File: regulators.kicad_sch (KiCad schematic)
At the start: 51 parts, among them SW1 SKRPANE010, U1 STM32H723ZGT6, U3 AP62300TWU, U4 AP2112K-3.3, Y1 25 MHz

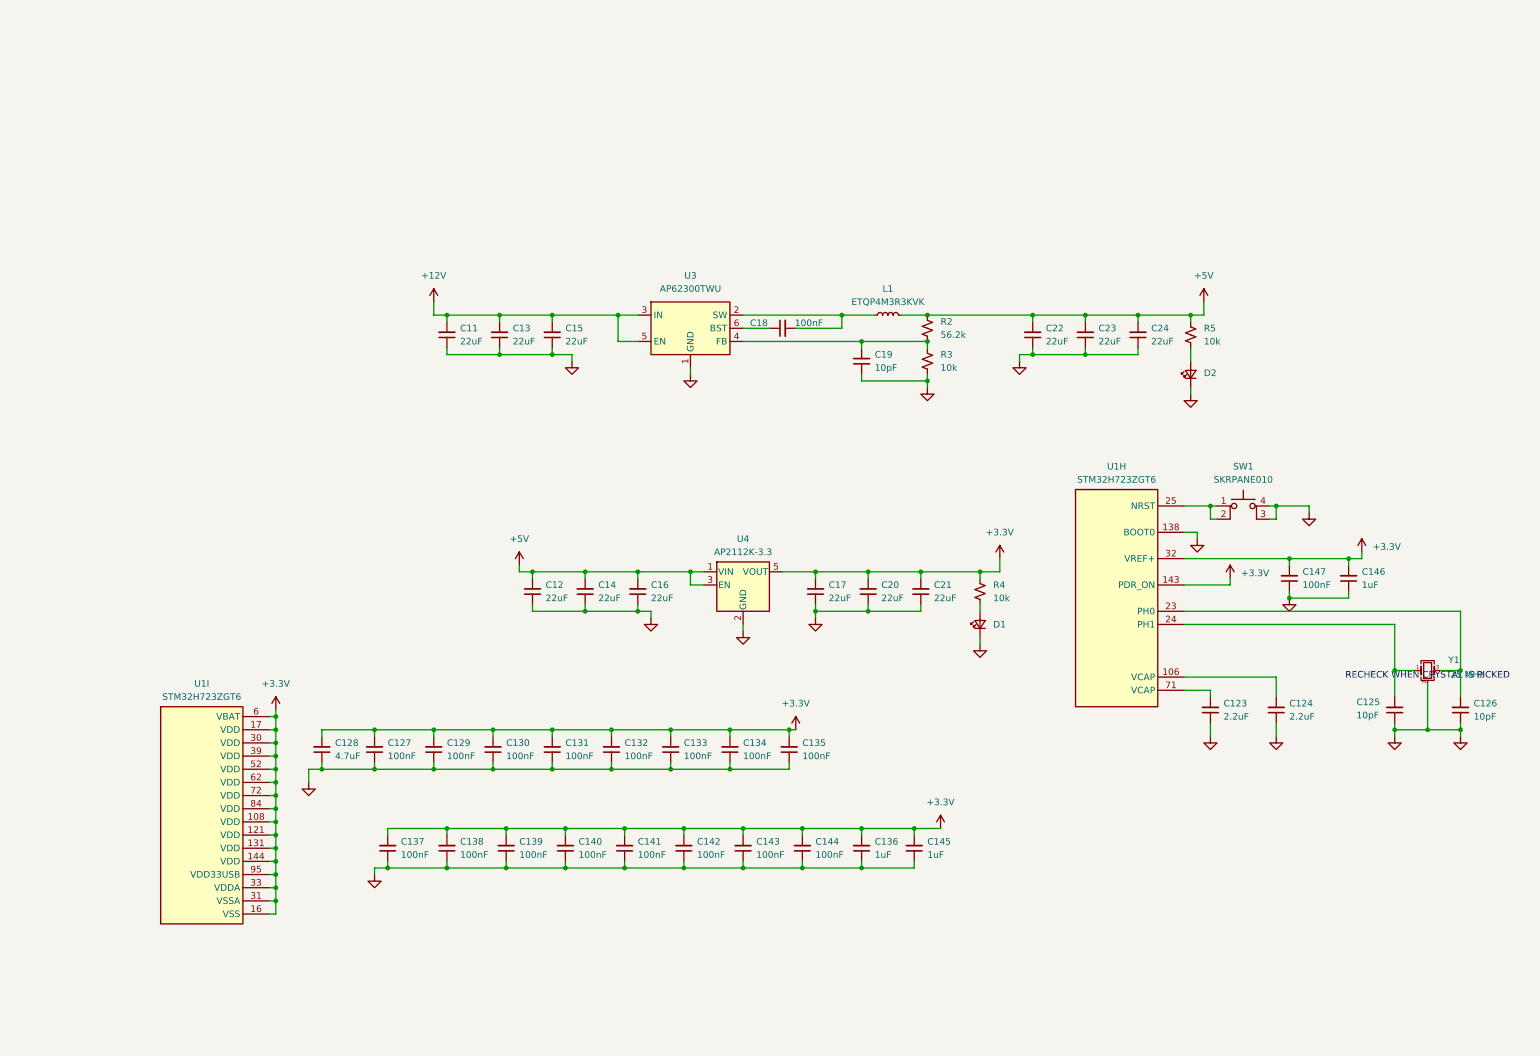
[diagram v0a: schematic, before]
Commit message: Soften scope, begin layout, reorganize sheets (still need to delete extras)
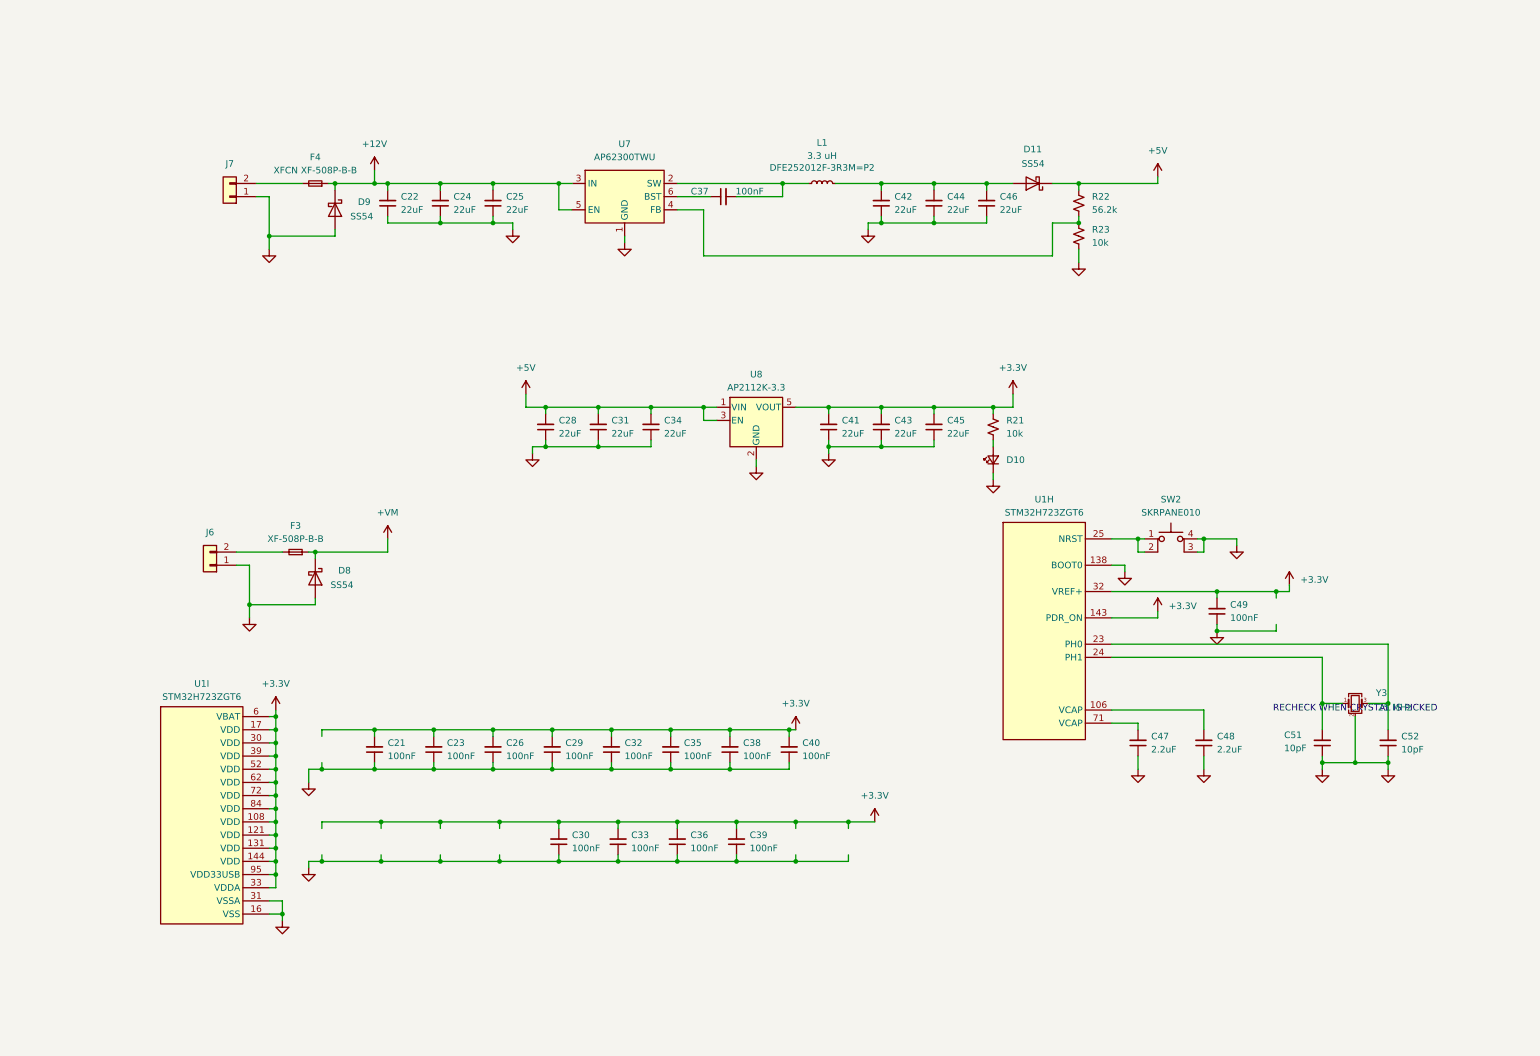
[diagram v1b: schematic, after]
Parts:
- removed C12, C14, C16, C17, C24: 22uF, symbol Device:C_Small
- removed C128: 4.7uF, symbol Device:C_Small
- removed C129, C137, C138, C139, C140: 100nF, symbol Device:C_Small
- removed C136, C145, C146: 1uF, symbol Device:C_Small
- removed C19: 10pF, symbol Device:C_Small
- removed D1, D2: LED_Small, symbol Device:LED_Small
- removed R4, R5: 10k, symbol Device:R_Small_US
- removed U3: AP62300TWU, Package_TO_SOT_SMD:TSOT-23-6, symbol Regulator_Switching:AP62300TWU
- removed U4: AP2112K-3.3, Package_TO_SOT_SMD:SOT-23-5, symbol Regulator_Linear:AP2112K-3.3
- added C23: 100nF, APRLPrints:C_0603, symbol Device:C_Small
- added C28, C31, C34, C41, C46: 22uF, APRLPrints:C_0805, symbol Device:C_Small
- added D10: LED_Small, APRLPrints:LED_0603, symbol Device:LED_Small
- added D11, D8, D9: SS54, Diode_SMD:D_SMA, symbol Diode:SS38
- added F3: XF-508P-B-B, Fuse:Fuseholder_Blade_Mini_Keystone_3568, symbol Device:Fuse_Small
- added F4: XFCN XF-508P-B-B, Fuse:Fuseholder_Blade_Mini_Keystone_3568, symbol Device:Fuse_Small
- added J6, J7: Screw_Terminal_01x02, Connector_Phoenix_MSTB:PhoenixContact_MSTBA_2,5_2-G_1x02_P5.00mm_Horizontal, symbol Connector_Generic:Conn_01x02
- added R21: 10k, APRLPrints:R_0603, symbol Device:R_Small_US
- added U7: AP62300TWU, Package_TO_SOT_SMD:TSOT-23-6, symbol Regulator_Switching:AP62300TWU
- added U8: AP2112K-3.3, Package_TO_SOT_SMD:SOT-23-5, symbol Regulator_Linear:AP2112K-3.3
- C21: renamed from C127; footprint (none) -> APRLPrints:C_0603
- C22: renamed from C11; footprint (none) -> APRLPrints:C_0805
- C24: renamed from C13; footprint (none) -> APRLPrints:C_0805
- C25: renamed from C15; footprint (none) -> APRLPrints:C_0805
- C26: renamed from C130; footprint (none) -> APRLPrints:C_0603
- C29: renamed from C131; footprint (none) -> APRLPrints:C_0603
- C30: renamed from C141; footprint (none) -> APRLPrints:C_0603
- C32: renamed from C132; footprint (none) -> APRLPrints:C_0603
- C33: renamed from C142; footprint (none) -> APRLPrints:C_0603
- C35: renamed from C133; footprint (none) -> APRLPrints:C_0603
- C36: renamed from C143; footprint (none) -> APRLPrints:C_0603
- C37: renamed from C18; footprint (none) -> APRLPrints:C_0603
- C38: renamed from C134; footprint (none) -> APRLPrints:C_0603
- C39: renamed from C144; footprint (none) -> APRLPrints:C_0603
- C40: renamed from C135; footprint (none) -> APRLPrints:C_0603
- C42: renamed from C22; footprint (none) -> APRLPrints:C_0805
- C43: renamed from C20; footprint (none) -> APRLPrints:C_0805
- C44: renamed from C23; footprint (none) -> APRLPrints:C_0805
- C45: renamed from C21; footprint (none) -> APRLPrints:C_0805
- C47: renamed from C123; footprint (none) -> APRLPrints:C_0603
- C48: renamed from C124; footprint (none) -> APRLPrints:C_0603
- C49: renamed from C147; footprint (none) -> APRLPrints:C_0603
- C51: renamed from C125; footprint (none) -> APRLPrints:C_0603
- C52: renamed from C126; footprint (none) -> APRLPrints:C_0603
- L1: value ETQP4M3R3KVK -> 3.3 uH; footprint Inductor_SMD:L_Panasonic_PCC-M0850M -> Inductor_SMD:L_1008_2520Metric; Part # (none) -> DFE252012F-3R3M=P2
- R22: renamed from R2; footprint (none) -> APRLPrints:R_0603
- R23: renamed from R3; footprint (none) -> APRLPrints:R_0603
- SW2: renamed from SW1; footprint (none) -> APRLPrints:SKRPANE010
- Y3: renamed from Y1; footprint (none) -> APRLPrints:3225-4P-L; private KLC_S4.1 -> (none)
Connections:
- net +12V: now also D9.1 (K), F4.1, U7.3 (IN), U7.5 (EN)
- net +3.3V: now also C23.2, C41.2, R21.1, U8.5 (VOUT); no longer U1.107 (VSS), U1.120 (VSS), U1.130 (VSS), U1.16 (VSS), U1.31 (VSSA), U1.38 (VSS), U1.51 (VSS), U1.61 (VSS), U1.83 (VSS), U1.94 (VSS)
- net +5V: now also C28.2, C31.2, C34.2, D11.1 (K), U8.1 (VIN), U8.3 (EN); no longer C42.2, C44.2, L1.2
- net GND: now also U1.107 (VSS), U1.120 (VSS), U1.130 (VSS), U1.16 (VSS), U1.31 (VSSA), U1.38 (VSS), U1.51 (VSS), U1.61 (VSS), U1.83 (VSS), U1.94 (VSS), C23.1, C28.1, C31.1, C34.1, C41.1, C46.1, D10.1 (K), D8.2 (A), D9.2 (A), J6.1 (Pin_1), J7.1 (Pin_1), U7.1 (GND), U8.2 (GND)
- net at R22.2, R23.1: now also U7.4 (FB)
- net at C37.1: now also U7.6 (BST)
- net at C37.2, L1.1: now also U7.2 (SW)
- new net: F3.2, J6.2 (Pin_2)
- new net: C42.2, C44.2, C46.2, D11.2 (A), L1.2
- new net: F4.2, J7.2 (Pin_2)
- new net: D10.2 (A), R21.2
- new net +VM: D8.1 (K), F3.1
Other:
- moved on the sheet: C22, C24, C25, C30, C33, C36, C37, C39, C42, C43, C44, C45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
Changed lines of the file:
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@@
 	(generator "eeschema")
 	(generator_version "9.0")
-	(paper "A4")
+	(paper "USLetter")
 	(title_block
 		(title "Serie Mainboard")

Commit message: ???
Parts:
- removed C21, C23, C26: 100nF, APRLPrints:C_0603, symbol Device:C_Small
- removed C22, C24, C25: 22uF, APRLPrints:C_0805, symbol Device:C_Small
- removed D11, D9: SS54, Diode_SMD:D_SMA, symbol Diode:SS38
- removed F4: XFCN XF-508P-B-B, Fuse:Fuseholder_Blade_Mini_Keystone_3568, symbol Device:Fuse_Small
- removed J6, J7: Screw_Terminal_01x02, Connector_Phoenix_MSTB:PhoenixContact_MSTBA_2,5_2-G_1x02_P5.00mm_Horizontal, symbol Connector_Generic:Conn_01x02
- removed L1: 3.3 uH, Inductor_SMD:L_1008_2520Metric, symbol Device:L_Small
- removed U1: STM32H723ZGT6, Package_QFP:LQFP-144_20x20mm_P0.5mm, symbol libserie:STM32H723ZGTx
- removed U7: AP62300TWU, Package_TO_SOT_SMD:TSOT-23-6, symbol Regulator_Switching:AP62300TWU
- removed U8: AP2112K-3.3, Package_TO_SOT_SMD:SOT-23-5, symbol Regulator_Linear:AP2112K-3.3
- added C27: 22uF, APRLPrints:C_0805, symbol Device:C_Small
- added C50: 100nF, symbol Device:C_Small
- added C53, C54, C56, C57, C59, C60, C61, C65: 22uF, symbol Device:C_Small
- added C55, C58, C62, C63, C64, C66, C67: 100nF, APRLPrints:C_0603, symbol Device:C_Small
- added D6: SS54, Diode_SMD:D_SMA, symbol Diode:SS38
- added D7, D9: LED_Small, APRLPrints:LED_0603, symbol Device:LED_Small
- added F2: XFCN XF-508P-B-B, Fuse:Fuseholder_Blade_Mini_Keystone_3568, symbol Device:Fuse_Small
- added J15: Screw_Terminal_06x01x02, TerminalBlock_Ningbo-Kagnex:TerminalBlock_Ningbo-Kagnex_HB9500M_1x12_P9.5mm, symbol libserie:Screw_Terminal_06x01x02
- added L1: 3.6 uH, symbol Device:L
- added L2: 10 uH, symbol Device:L
- added R18, R19: 200k, symbol Device:R_Small_US
- added R20: 15.8k, symbol Device:R_Small_US
- added R24, R26: 22.1k, symbol Device:R_Small_US
- added R25: 309k, symbol Device:R_Small_US
- added R27, R28: 10k, APRLPrints:R_0603, symbol Device:R_Small_US
- added U13: STM32H723ZGT6, Package_QFP:LQFP-144_20x20mm_P0.5mm, symbol libserie:STM32H723ZGTx
- added U14: AP2112K-3.3, Package_TO_SOT_SMD:SOT-23-5, symbol Regulator_Linear:AP2112K-3.3
- added U15, U16: AP64500, Package_SO:Diodes_SO-8EP, symbol libserie:AP64500-EP
- added U17: TPS7A20xxxDQN, Package_SON:Texas_X2SON-4_1x1mm_P0.65mm, symbol Regulator_Linear:TPS7A20xxxDQN
- C28, C31: value 22uF -> 2.2uF; footprint APRLPrints:C_0805 -> APRLPrints:C_0603
- C29, C30, C38: value 100nF -> 22uF; footprint APRLPrints:C_0603 -> APRLPrints:C_0805
- C33, C36, C37, C40: value 100nF -> 22uF; footprint APRLPrints:C_0603 -> (none)
- C34, C41: footprint APRLPrints:C_0805 -> (none)
- C35, C39: value 100nF -> 10pF
- C44, C45: value 22uF -> 2.7nF; footprint APRLPrints:C_0805 -> (none)
- C46: value 22uF -> 100nF; footprint APRLPrints:C_0805 -> APRLPrints:C_0603
- C47, C48: value 2.2uF -> 100nF
- C49: footprint APRLPrints:C_0603 -> (none)
- C51, C52: value 10pF -> 100nF
- R21: value 10k -> 37.4k; footprint APRLPrints:R_0603 -> (none)
- R22: value 56.2k -> 10k
- R23: value 10k -> 115k; footprint APRLPrints:R_0603 -> (none)
- Y1: renamed from Y3; private (none) -> KLC_S4.1
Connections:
- net +12V: now also C54.1, C57.1, C60.1, L2.2, R25.1, R28.1
- net +3.3V: now also C42.2, C46.2, C47.2, C48.2, C51.2, C52.2, R22.1, C55.2, C58.2, C62.2, C63.2, C64.2, C66.2, C67.2, U13.41 (PA5), U13.43 (PA7), U14.5 (VOUT); no longer C29.2, C30.2, C33.2, C35.2, C36.2, C39.2, C40.2, C41.2, C45.2, C49.2, R21.1
- net +5V: now also C29.2, C30.2, R23.1, C27.2, C53.1, C56.1, C59.1, C61.1, L1.2, R27.1, U14.1 (VIN), U14.3 (EN), U17.3 (EN), U17.4 (IN); no longer C28.2, C31.2, C34.2, R22.1
- net GND: now also C33.2, C34.2, C36.2, C37.2, C40.2, C41.2, C44.2, C45.2, C27.1, C53.2, C54.2, C55.1, C56.2, C57.2, C58.1, C59.2, C60.2, C61.2, C62.1, C63.1, C64.1, C65.2, C66.1, C67.1, D6.2 (A), D7.1 (K), D9.1 (K), J15.1 (Pin_1), J15.3 (Pin_1), R18.2, R19.2, R24.2, R26.2, U13.37 (PA3), U14.2 (GND), U15.7 (GND), U15.9 (EP), U16.7 (GND), U16.9 (EP), U17.2 (GND), U17.5 (Pad); no longer C33.1, C34.1, C36.1, C40.1, C41.1, C44.1, C45.1, C49.1, R23.2
- net at R22.2: now also D7.2 (A); no longer R23.1
- net at F3.2: now also J15.4 (Pin_2)
- net at Y1.1: now also C35.2, U13.102 (PA10); no longer C51.2
- net +24V: now reaches C37.1
- net +24V: now also C33.1, C34.1, C36.1, C40.1, C41.1, D6.1 (K), F2.1, U15.2 (VIN), U15.3 (EN), U16.2 (VIN), U16.3 (EN)
- net at SW2.1, SW2.2: now also U13.35 (PA1)
- net at Y1.3: now also C39.2, U13.101 (PA9); no longer C52.2
- net at R21.2: now also C45.1; no longer D10.2 (A)
- new net: C49.2, L1.1, U15.8 (SW)
- new net: R23.2, R24.1, U15.5 (FB)
- new net: D10.2 (A), R28.2
- new net: D9.2 (A), R27.2
- new net: C49.1, U15.1 (BST)
- new net: R18.1, U15.4 (RT/CLK)
- new net: R20.1, U15.6 (COMP)
- new net: C44.1, R20.2
- new net: C31.2, U13.109 (PA14(JTCK)
- new net: C28.2, U13.110 (PA15(JTDI))
- new net: R19.1, U16.4 (RT/CLK)
- new net: R21.1, U16.6 (COMP)
- new net: F2.2, J15.2 (Pin_2)
- new net: R25.2, R26.1, U16.5 (FB)
- new net: C50.1, U16.1 (BST)
- new net: C50.2, L2.1, U16.8 (SW)
- new net +4.5V: C65.1, U17.1 (OUT)
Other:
- note added: "24V -> 12V"
- note added: "24V -> 5V"
- note added: "3.3V Regulator"
- note added: "Motor Power"
- note added: "Power Inputs"
- note added: "Power Regulators"
- note added: "Precision 4.5V Regulator"
- note added: "This still needs a home"
- note removed: "RECHECK WHEN CRYSTAL IS PICKED"
- moved on the sheet: SW2, Y1

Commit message: loadcell math coming soon(tm)
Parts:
- removed C28, C31: 2.2uF, APRLPrints:C_0603, symbol Device:C_Small
- removed C32: 100nF, APRLPrints:C_0603, symbol Device:C_Small
- removed C35, C39: 10pF, APRLPrints:C_0603, symbol Device:C_Small
- removed unit 2 of J15
- removed SW2: SKRPANE010, APRLPrints:SKRPANE010, symbol Switch:SW_MEC_5E
- removed U13: STM32H723ZGT6, Package_QFP:LQFP-144_20x20mm_P0.5mm, symbol libserie:STM32H723ZGTx
- removed Y1: 25 MHz, APRLPrints:3225-4P-L, symbol Device:Crystal_GND24_Small
- added D20: SS54, Diode_SMD:D_SMA, symbol Diode:SS38
- added unit 2 of J14
- C32: renamed from C50; footprint (none) -> APRLPrints:C_0603
- C33: renamed from C34; footprint (none) -> APRLPrints:C_0805
- C34: renamed from C37; footprint (none) -> APRLPrints:C_0805
- C35: renamed from C41; footprint (none) -> APRLPrints:C_0805
- C36: renamed from C54; footprint (none) -> APRLPrints:C_0805
- C37: renamed from C57; footprint (none) -> APRLPrints:C_0805
- C38: renamed from C60; footprint (none) -> APRLPrints:C_0805
- C39: renamed from C45; value 2.7nF -> 1nF; footprint (none) -> APRLPrints:C_0603
- C40: renamed from C49; footprint (none) -> APRLPrints:C_0603
- C41: renamed from C33; footprint (none) -> APRLPrints:C_0805
- C42: renamed from C36; footprint (none) -> APRLPrints:C_0805
- C43: renamed from C40; footprint (none) -> APRLPrints:C_0805
- C44: renamed from C53; footprint (none) -> APRLPrints:C_0805
- C45: renamed from C56; footprint (none) -> APRLPrints:C_0805
- C46: renamed from C59; footprint (none) -> APRLPrints:C_0805
- C47: renamed from C44; value 2.7nF -> 1nF; footprint (none) -> APRLPrints:C_0603
- C54: renamed from C61; footprint (none) -> APRLPrints:C_0805
- C55: renamed from C65; footprint (none) -> APRLPrints:C_0805
- L1: renamed from L2; value 10 uH -> 6.8 uH; footprint (none) -> Inductor_SMD:L_Changjiang_FXL0630; Part # SLO1040H100MTT -> FXL0630-6R8-M
- L2: renamed from L1; value 3.6 uH -> 3.3 uH; footprint (none) -> Inductor_SMD:L_Changjiang_FXL0630; Part # GDIM1070-3R6MTF -> FXL0630-3R3-M
- R31: renamed from R25; value 309k -> 140k; footprint (none) -> APRLPrints:R_0603
- R32: renamed from R19; footprint (none) -> APRLPrints:R_0603
- R33: renamed from R21; value 37.4k -> 30.9k; footprint (none) -> APRLPrints:R_0603
- R34: renamed from R26; value 22.1k -> 10k; footprint (none) -> APRLPrints:R_0603
- R36: renamed from R23; value 115k -> 52.5k; footprint (none) -> APRLPrints:R_0603
- R37: renamed from R18; footprint (none) -> APRLPrints:R_0603
- R38: renamed from R20; value 15.8k -> 30.9k; footprint (none) -> APRLPrints:R_0603
- R39: renamed from R24; value 22.1k -> 10k; footprint (none) -> APRLPrints:R_0603
- renumbered C27 to C48, C29 to C49, C30 to C50, C38 to C51, C42 to C52, C43 to C53, C46 to C56, C47 to C57, C48 to C58, C51 to C59, C52 to C60, C55 to C61, C58 to C62, C62 to C63, C63 to C64, C64 to C65, D7 to D10, D10 to D7, D9 to D8, D8 to D9, J15 to J14, R28 to R30, R27 to R35, R22 to R40, U16 to U12, U15 to U13, U17 to U15
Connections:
- net +5V: now also D20.1 (K); no longer C44.1, C45.1, C46.1, L2.2
- net GND: now also J14.3 (Pin_1)
- net at F3.2: now also J14.4 (Pin_2)
- new net: C44.1, C45.1, C46.1, D20.2 (A), L2.2
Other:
- note removed: "This still needs a home"
- moved on the sheet: C48, C49, C50, C51, C52, C53, C54, C55, C56, C57, C58, C59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

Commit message: a
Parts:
- removed D6, D9: SS54, Diode_SMD:D_SMA, symbol Diode:SS38
- removed U12: AP64500, Package_SO:Diodes_SO-8EP, symbol libserie:AP64500-EP
- added C32, C42: 100uF, Capacitor_SMD:CP_Elec_10x10.5, symbol Device:C_Small
- added C36, C46, C56, C58, C59: 100nF, APRLPrints:C_0603, symbol Device:C_Small
- added C57: 1uF, APRLPrints:C_0603, symbol Device:C_Small
- added Q1, Q2, Q3: BSC016N06NS, Package_TO_SOT_SMD:TDSON-8-1, symbol Transistor_FET:CSD18532NQ5B
- added U11: AP64500, libserie:Diodes_SO-8EP, symbol libserie:AP64500-EP
- added U12, U14, U17: AP74700Q, libserie:SOT-6, symbol libserie:AP74700Q
- F2: value XFCN XF-508P-B-B -> XF-508P-B-B
- U13: footprint Package_SO:Diodes_SO-8EP -> libserie:Diodes_SO-8EP
- U15: renamed from U14; value AP2112K-3.3 -> TLV77533
- renumbered C32 to C28, C33 to C29, C34 to C30, C35 to C31, C37 to C33, C38 to C34, C36 to C35, C39 to C37, C40 to C38, C41 to C39, C42 to C40, C43 to C41, C45 to C43, C46 to C44, C44 to C45, C56 to C60, C57 to C61, C58 to C62, C59 to C63, C60 to C64, C61 to C65, C62 to C66, C63 to C67, C64 to C68, C65 to C69, C66 to C70, C67 to C71, D7 to D6, D20 to D7, D10 to D9, J14 to J10, R30 to R23, R31 to R24, R34 to R25, R32 to R26, R33 to R27, R35 to R28, R36 to R29, R37 to R30, R39 to R31, R38 to R32, R40 to R33, U15 to U16
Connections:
- net +12V: now also C32.1
- net +24V: now also Q1.5 (D), U11.2 (VIN), U11.3 (EN), U12.4 (CATHODE); no longer F2.1
- net +3.3V: now also C57.2, C58.2, C59.2
- net +5V: now also Q2.5 (D), U14.4 (CATHODE); no longer D7.1 (K), R28.1, R29.1
- net GND: now also J10.1 (Pin_1), J10.3 (Pin_1), C32.2, C42.2, C57.1, C58.1, C59.1, U11.7 (GND), U11.9 (EP), U12.2 (GND), U14.2 (GND), U17.2 (GND); no longer J10.1 (Pin_1), J10.3 (Pin_1)
- net at L2.1, U13.8 (SW): now also C38.1; no longer C38.2
- net at C43.1, C44.1, C45.1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: now also C42.1
- net at U13.1 (BST): now also C38.2; no longer C38.1
- net at F3.2: now also J10.2 (Pin_2); no longer J10.4 (Pin_2)
- net at R26.1: now also U11.4 (RT/CLK)
- net at R27.1: now also U11.6 (COMP)
- net at F2.2: now also J10.4 (Pin_2), C36.2, U12.3 (EN), U12.6 (ANODE); no longer J10.2 (Pin_2)
- net at R24.2, R25.1: now also U11.5 (FB)
- net at C28.1: now also L1.1, U11.8 (SW)
- net at C28.2: now also U11.1 (BST); no longer L1.1
- net +VM: no longer names the net of F3.1
- net +VM: now also C56.2, Q3.1 (S), Q3.2 (S), Q3.3 (S), U17.3 (EN), U17.6 (ANODE)
- new net: C46.2, D7.1 (K), Q2.1 (S), Q2.2 (S), Q2.3 (S), R28.1, R29.1, U14.3 (EN), U14.6 (ANODE)
- new net: Q2.4 (G), U14.5 (GATE)
- new net: C56.1, U17.1 (VCP)
- new net: F2.1, Q1.1 (S), Q1.2 (S), Q1.3 (S)
- new net: Q1.4 (G), U12.5 (GATE)
- new net: C36.1, U12.1 (VCP)
- new net: C46.1, U14.1 (VCP)
- new net: Q3.4 (G), U17.5 (GATE)
- new net VM: Q3.5 (D), U17.4 (CATHODE)
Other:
- moved on the sheet: C28, C29, C30, C31, C33, C34, C35, C37, C38, C39, C40, C41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
